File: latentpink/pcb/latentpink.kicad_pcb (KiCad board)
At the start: 8 copper layers, 145 x 139 mm, 563 parts, among them J1 CONN_SFP_HOST, J10 XILINX_JTAG, J13 CONN_01X05, J14 CONN_01X03, J15 CONN_01X03, J16 JUMPER_0402_SPDT, J17 JUMPER_0402_SPDT, J18 BEL_FUSE_0845-2R1T-E4, J19 BEL_FUSE_0845-2R1T-E4, J2 SFP_CAGE, J20 BEL_FUSE_0845-2R1T-E4, J21 BEL_FUSE_0845-2R1T-E4, J22 BEL_FUSE_0845-2R1T-E4, J3 XILINX_JTAG, J4 BEL_FUSE_0845-2R1T-E4, J5 0826-1G1T-23-F, J6 BARREL_JACK, J7 RJ45, J8 BEL_FUSE_0845-2R1T-E4, J9 XILINX_JTAG, M1 960-27-12-D-AB-0, M2 960-23-23-F-AB-0, M3 SCREWHOLE, M4 SCREWHOLE, M5 SCREWHOLE, M6 SCREWHOLE, U1 VSC8512, U10 MYMGK1R812ERSR, U11 MYMGK00504ERSR, U12 STM32L031-QFN32, U13 MYMGK00504ERSR, U14 MYMGK00504ERSR, U15 MYMGK00504ERSR, U16 NCP45521IMNTWG-H, U17 NCP45521IMNTWG-H, U18 LP2996AMRE, U19 TPS7A2533DRVR, U2 XC7K160T-2FBG484C, U20 AT24MAC402, U21 ECX2-LMV-3CN-125.000-TR, U22 ECS-2016MVQ-250-CN, U23 ADM3101E_QFN, U3 CY7C2245KV18-450BZXI, U4 STM32H735-UFBGA176-25, U5 DP83867, U6 DP83867, U9 KSZ9031RN

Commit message: Continued footprint assignment and miscellaneous missing tidbits of schematic
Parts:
- added C1: 330 uF, azonenberg_pcb:EIA_1210_CAP_NOSILK, F.Cu at (253.6, 36.1)
- added C100: 22 uF 25V, azonenberg_pcb:EIA_1812_CAP_NOSILK, F.Cu at (233.7, 72.2)
- added C101: 22 uF 25V, azonenberg_pcb:EIA_1812_CAP_NOSILK, F.Cu at (247.6, 56.2)
- added C102: 22 uF 25V, azonenberg_pcb:EIA_1812_CAP_NOSILK, F.Cu at (233.7, 56.2)
- added C103: 22 uF 25V, azonenberg_pcb:EIA_1812_CAP_NOSILK, F.Cu at (240.7, 56.2)
- added C104: 22 uF 25V, azonenberg_pcb:EIA_1812_CAP_NOSILK, F.Cu at (233.7, 60.2)
- added C105: 22 uF 25V, azonenberg_pcb:EIA_1812_CAP_NOSILK, F.Cu at (233.7, 68.2)
- added C107: 220 uF, azonenberg_pcb:EIA_1210_CAP_NOSILK, F.Cu at (232.6, 43.9)
- added C108: 220 uF, azonenberg_pcb:EIA_1210_CAP_NOSILK, F.Cu at (244.7, 72.0)
- added C109: 220 uF, azonenberg_pcb:EIA_1210_CAP_NOSILK, F.Cu at (246.6, 64.1)
- added C112: 220 uF, azonenberg_pcb:EIA_1210_CAP_NOSILK, F.Cu at (253.6, 56.1)
- added C113: 220 uF, azonenberg_pcb:EIA_1210_CAP_NOSILK, F.Cu at (234.5, 36.1)
- added C114: 220 uF, azonenberg_pcb:EIA_1210_CAP_NOSILK, F.Cu at (253.6, 60.0)
- added C117: EEH-ZS1E102UV, azonenberg_pcb:CAP_AL_10MM_SMT, F.Cu at (13.5, 24.3)
- added C118: DNP, azonenberg_pcb:CAP_AL_10MM_SMT, F.Cu at (13.4, 39.9)
- added C120: DNP, azonenberg_pcb:CAP_AL_10MM_SMT, F.Cu at (25.6, 39.9)
- added C122: EEH-ZS1E102UV, azonenberg_pcb:CAP_AL_10MM_SMT, F.Cu at (25.7, 24.3)
- added C154: 330 uF, azonenberg_pcb:EIA_1210_CAP_NOSILK, F.Cu at (237.7, 79.8)
- added C155: 47 uF, azonenberg_pcb:EIA_1210_CAP_NOSILK, F.Cu at (232.7, 83.7)
- added C157: 47 uF, azonenberg_pcb:EIA_1210_CAP_NOSILK, F.Cu at (232.7, 79.8)
- added C158: 330 uF, azonenberg_pcb:EIA_1210_CAP_NOSILK, F.Cu at (237.7, 83.7)
- added C159: 47 uF, azonenberg_pcb:EIA_1210_CAP_NOSILK, F.Cu at (242.7, 79.8)
- added C228: 0.47 uF, azonenberg_pcb:EIA_0402_CAP_NOSILK, F.Cu at (250.6, 48.0)
- added C229: 0.47 uF, azonenberg_pcb:EIA_0402_CAP_NOSILK, F.Cu at (215.7, 63.0)
- added C234: 4.7 uF, azonenberg_pcb:EIA_0603_CAP_NOSILK, F.Cu at (247.7, 46.7)
- added C241: 0.47 uF, azonenberg_pcb:EIA_0402_CAP_NOSILK, F.Cu at (250.6, 46.5)
- added C289: 47 uF, azonenberg_pcb:EIA_1210_CAP_NOSILK, F.Cu at (248.6, 36.1)
- added C301: 47 uF, azonenberg_pcb:EIA_1210_CAP_NOSILK, F.Cu at (253.6, 40.0)
- added C447: 0.47 uF, azonenberg_pcb:EIA_0402_CAP_NOSILK, F.Cu at (216.9, 60.6)
- added C448: 0.47 uF, azonenberg_pcb:EIA_0402_CAP_NOSILK, F.Cu at (193.8, 55.0)
- added C449: 0.47 uF, azonenberg_pcb:EIA_0402_CAP_NOSILK, F.Cu at (195.9, 61.1)
- added C450: 0.1 uF, azonenberg_pcb:EIA_0402_CAP_NOSILK, F.Cu at (139.3, 44.6)
- added C451: 0.1 uF, azonenberg_pcb:EIA_0402_CAP_NOSILK, F.Cu at (136.8, 41.6)
- added C452: 0.1 uF, azonenberg_pcb:EIA_0402_CAP_NOSILK, F.Cu at (139.3, 43.1)
- added C453: 0.1 uF, azonenberg_pcb:EIA_0402_CAP_NOSILK, F.Cu at (136.8, 44.6)
- added C454: 0.1 uF, azonenberg_pcb:EIA_0402_CAP_NOSILK, F.Cu at (141.8, 43.1)
- added C455: 0.1 uF, azonenberg_pcb:EIA_0402_CAP_NOSILK, F.Cu at (136.8, 43.1)
- added C456: 0.1 uF, azonenberg_pcb:EIA_0402_CAP_NOSILK, F.Cu at (141.8, 41.6)
- added C457: 0.1 uF, azonenberg_pcb:EIA_0402_CAP_NOSILK, F.Cu at (139.3, 41.6)
- added C458: 0.47 uF, azonenberg_pcb:EIA_0402_CAP_NOSILK, F.Cu at (189.8, 36.2)
- added C459: 0.47 uF, azonenberg_pcb:EIA_0402_CAP_NOSILK, F.Cu at (187.3, 36.2)
- added C460: 0.47 uF, azonenberg_pcb:EIA_0402_CAP_NOSILK, F.Cu at (187.3, 37.7)
- added C461: 0.47 uF, azonenberg_pcb:EIA_0402_CAP_NOSILK, F.Cu at (192.3, 34.7)
- added C462: 0.47 uF, azonenberg_pcb:EIA_0402_CAP_NOSILK, F.Cu at (187.3, 34.7)
- added C463: 0.47 uF, azonenberg_pcb:EIA_0402_CAP_NOSILK, F.Cu at (189.8, 37.7)
- added C464: 0.47 uF, azonenberg_pcb:EIA_0402_CAP_NOSILK, F.Cu at (187.3, 39.2)
- added C465: 0.47 uF, azonenberg_pcb:EIA_0402_CAP_NOSILK, F.Cu at (189.8, 34.7)
- added C466: 0.47 uF, azonenberg_pcb:EIA_0402_CAP_NOSILK, F.Cu at (238.1, 107.9)
- added C467: 0.1 uF, azonenberg_pcb:EIA_0402_CAP_NOSILK, F.Cu at (238.1, 109.4)
- added C468: 0.1 uF, azonenberg_pcb:EIA_0402_CAP_NOSILK, F.Cu at (235.6, 109.4)
- added C469: 0.1 uF, azonenberg_pcb:EIA_0402_CAP_NOSILK, F.Cu at (229.6, 114.8)
- added C470: 0.1 uF, azonenberg_pcb:EIA_0402_CAP_NOSILK, F.Cu at (232.1, 114.8)
- added C471: 22 uF, azonenberg_pcb:EIA_1206_CAP_NOSILK, F.Cu at (227.2, 108.4)
- added C472: 22 uF, azonenberg_pcb:EIA_1206_CAP_NOSILK, F.Cu at (227.2, 111.0)
- added C473: 0.1 uF, azonenberg_pcb:EIA_0402_CAP_NOSILK, F.Cu at (234.6, 112.5)
- added C474: 0.1 uF, azonenberg_pcb:EIA_0402_CAP_NOSILK, F.Cu at (225.9, 115.3)
- added C475: DNP, azonenberg_pcb:EIA_1210_CAP_NOSILK, F.Cu at (239.7, 68.1)
- added C476: DNP, azonenberg_pcb:EIA_1210_CAP_NOSILK, F.Cu at (249.7, 68.0)
- added C6: 47 uF, azonenberg_pcb:EIA_1206_CAP_NOSILK, F.Cu at (248.6, 39.4)
- added C67: 47 uF, azonenberg_pcb:EIA_1210_CAP_NOSILK, F.Cu at (240.0, 30.0)
- added C89: 22 uF 25V, azonenberg_pcb:EIA_1812_CAP_NOSILK, F.Cu at (240.7, 64.2)
- added C90: 22 uF 25V, azonenberg_pcb:EIA_1812_CAP_NOSILK, F.Cu at (240.7, 60.2)
- added C91: 220 uF, azonenberg_pcb:EIA_1210_CAP_NOSILK, F.Cu at (251.6, 64.1)
- added C92: 220 uF, azonenberg_pcb:EIA_1210_CAP_NOSILK, F.Cu at (239.7, 72.0)
- added C93: 220 uF, azonenberg_pcb:EIA_1210_CAP_NOSILK, F.Cu at (239.5, 36.1)
- added C94: 22 uF 25V, azonenberg_pcb:EIA_1812_CAP_NOSILK, F.Cu at (233.7, 64.2)
- added C95: 22 uF 25V, azonenberg_pcb:EIA_1812_CAP_NOSILK, F.Cu at (247.6, 60.2)
- added C96: 220 uF, azonenberg_pcb:EIA_1210_CAP_NOSILK, F.Cu at (244.7, 68.1)
- added C97: 220 uF, azonenberg_pcb:EIA_1210_CAP_NOSILK, F.Cu at (234.5, 40.0)
- added C98: 10 uF 25V, azonenberg_pcb:EIA_1210_CAP_NOSILK, F.Cu at (251.5, 79.8)
- added C99: 10 uF 25V, azonenberg_pcb:EIA_1210_CAP_NOSILK, F.Cu at (256.5, 79.8)
- added D5: GREEN, azonenberg_pcb:EIA_0603_LED, F.Cu at (214.0, 61.1)
- added D6: GREEN, azonenberg_pcb:EIA_0603_LED, F.Cu at (226.8, 120.4)
- added D7: GREEN, azonenberg_pcb:EIA_0603_LED, F.Cu at (226.8, 122.7)
- added J11: FAN_01, azonenberg_pcb:CONN_MOLEX_KK_0470531000, F.Cu at (107.4, 11.9)
- added J12: FAN_01, azonenberg_pcb:CONN_MOLEX_KK_0470531000, F.Cu at (95.2, 11.9)
- added L6: 4.7 uH, azonenberg_pcb:EIA_0805_INDUCTOR_NOSILK, F.Cu at (226.5, 113.5)
- added L7: 4.7 uH, azonenberg_pcb:EIA_0805_INDUCTOR_NOSILK, F.Cu at (231.5, 112.9)
- added M10: WEEE, w_logo:Logo_silk_WEEE_3.4x5mm, F.Cu at (229.5, 101.5)
- added M7: LONGTHING, azonenberg_pcb:LONGTHING-1200DPI, F.Cu at (222.7, 96.4)
- added M8: OSHW, w_logo:Logo_silk_OSHW_6x6mm, F.Cu at (230.5, 94.6)
- added M9: POLARITY, w_logo:Logo_silk_polarity_center_5x1.4mm, F.Cu at (220.1, 101.3)
- added R117: 100, azonenberg_pcb:EIA_0402_RES_NOSILK, F.Cu at (202.9, 61.1)
- added R118: 100, azonenberg_pcb:EIA_0402_RES_NOSILK, F.Cu at (202.9, 62.6)
- added R122: DNP, azonenberg_pcb:EIA_1206_CAP_NOSILK, F.Cu at (203.9, 35.2)
- added R123: 33, azonenberg_pcb:EIA_0402_RES_NOSILK, F.Cu at (207.1, 47.5)
- added R124: 33, azonenberg_pcb:EIA_0402_RES_NOSILK, F.Cu at (191.3, 55.0)
- added R125: 33, azonenberg_pcb:EIA_0402_RES_NOSILK, F.Cu at (193.8, 56.5)
- added R126: 33, azonenberg_pcb:EIA_0402_RES_NOSILK, F.Cu at (198.8, 55.0)
- added R127: 4.7K, azonenberg_pcb:EIA_0402_RES_NOSILK, F.Cu at (202.4, 52.1)
- added R128: 4.7K, azonenberg_pcb:EIA_0402_RES_NOSILK, F.Cu at (202.4, 53.6)
- added R129: 4.7K, azonenberg_pcb:EIA_0402_RES_NOSILK, F.Cu at (191.3, 56.5)
- added R130: 100, azonenberg_pcb:EIA_0402_RES_NOSILK, F.Cu at (195.9, 62.6)
- added R131: 100, azonenberg_pcb:EIA_0402_RES_NOSILK, F.Cu at (196.3, 55.0)
- added R132: 4.7K, azonenberg_pcb:EIA_0402_RES_NOSILK, F.Cu at (194.8, 34.7)
- added R133: 4.7K, azonenberg_pcb:EIA_0402_RES_NOSILK, F.Cu at (192.3, 36.2)
- added R134: 0.1, azonenberg_pcb:EIA_0402_RES_NOSILK, F.Cu at (235.6, 110.9)
- added R135: 0.5, azonenberg_pcb:EIA_0402_RES_NOSILK, F.Cu at (235.6, 107.9)
- added R136: 0.5, azonenberg_pcb:EIA_0402_RES_NOSILK, F.Cu at (234.6, 114.0)
- added R137: 5.76K, azonenberg_pcb:EIA_0402_RES_NOSILK, F.Cu at (228.4, 126.1)
- added R138: 2.49K, azonenberg_pcb:EIA_0402_RES_NOSILK, F.Cu at (230.9, 124.4)
- added R139: 10K, azonenberg_pcb:EIA_0402_RES_NOSILK, F.Cu at (232.2, 121.4)
- added R140: 2.49K, azonenberg_pcb:EIA_0402_RES_NOSILK, F.Cu at (225.9, 124.6)
- added R141: 5.76K, azonenberg_pcb:EIA_0402_RES_NOSILK, F.Cu at (234.7, 122.9)
- added R142: 2.49K, azonenberg_pcb:EIA_0402_RES_NOSILK, F.Cu at (229.7, 122.9)
- added R143: 10K, azonenberg_pcb:EIA_0402_RES_NOSILK, F.Cu at (237.2, 121.4)
- added R144: 2.49K, azonenberg_pcb:EIA_0402_RES_NOSILK, F.Cu at (230.9, 125.9)
- added R145: 10K, azonenberg_pcb:EIA_0402_RES_NOSILK, F.Cu at (229.7, 119.9)
- added R146: 2.49K, azonenberg_pcb:EIA_0402_RES_NOSILK, F.Cu at (233.4, 124.4)
- added R147: 10K, azonenberg_pcb:EIA_0402_RES_NOSILK, F.Cu at (234.7, 119.9)
- added R148: 2.49K, azonenberg_pcb:EIA_0402_RES_NOSILK, F.Cu at (237.2, 119.9)
- added R149: 470, azonenberg_pcb:EIA_0402_RES_NOSILK, F.Cu at (228.4, 124.6)
- added R150: 470, azonenberg_pcb:EIA_0402_RES_NOSILK, F.Cu at (229.7, 121.4)
- added R151: 470, azonenberg_pcb:EIA_0402_RES_NOSILK, F.Cu at (232.2, 122.9)
- added R152: 470, azonenberg_pcb:EIA_0402_RES_NOSILK, F.Cu at (234.7, 121.4)
- added R153: 470, azonenberg_pcb:EIA_0402_RES_NOSILK, F.Cu at (225.9, 126.1)
- added R154: 470, azonenberg_pcb:EIA_0402_RES_NOSILK, F.Cu at (232.2, 119.9)
- added R53: 470, azonenberg_pcb:EIA_0402_RES_NOSILK, F.Cu at (213.2, 63.0)
- added TP19: TESTPOINT, azonenberg_pcb:TESTPOINT_SMT_0.5MM, F.Cu at (222.8, 60.6)
- added TP20: TESTPOINT, azonenberg_pcb:TESTPOINT_SMT_0.5MM, F.Cu at (222.8, 62.1)
- added TP21: TESTPOINT, azonenberg_pcb:TESTPOINT_SMT_0.5MM, F.Cu at (204.9, 61.1)
- added TP22: TESTPOINT, azonenberg_pcb:TESTPOINT_SMT_0.5MM, F.Cu at (204.9, 62.6)
- added TP23: U.FL, azonenberg_pcb:CONN_U.FL_TE_1909763-1, F.Cu at (225.8, 49.3)
- added TP24: U.FL, azonenberg_pcb:CONN_U.FL_TE_1909763-1, F.Cu at (214.7, 49.3)
- added TP25: U.FL, azonenberg_pcb:CONN_U.FL_TE_1909763-1, F.Cu at (220.3, 49.3)
- added U24: SIT9121AI-2BF-XXS200.000000G, azonenberg_pcb:OSCILLATOR_LVDS_3.2x2.5, F.Cu at (105.4, 76.6)
- added U25: SIT9121AI-2BF-XXS156.250000G, azonenberg_pcb:OSCILLATOR_LVDS_3.2x2.5, F.Cu at (100.8, 76.6)
- added U26: 74LVC1T45, azonenberg_pcb:DFN_6_0.5MM_1.45x1.00MM, F.Cu at (87.7, 134.2)
- added U27: 74LVC1T45, azonenberg_pcb:DFN_6_0.5MM_1.45x1.00MM, F.Cu at (90.2, 134.2)
- added U28: IS25WP256D-JLLE, azonenberg_pcb:DFN_8_1.27MM_8x6MM, F.Cu at (195.6, 50.5)
- added U29: DSC1123CI2-150.0000T, azonenberg_pcb:OSCILLATOR_LVDS_3.2x2.5, F.Cu at (203.5, 49.1)
- added U30: DSC1123CI2-150.0000T, azonenberg_pcb:OSCILLATOR_LVDS_3.2x2.5, F.Cu at (192.4, 62.7)
- added U31: 74LVC1T45, azonenberg_pcb:DFN_6_0.5MM_1.45x1.00MM, F.Cu at (194.9, 38.6)
- added U32: 74LVC1T45, azonenberg_pcb:DFN_6_0.5MM_1.45x1.00MM, F.Cu at (194.9, 36.4)
- added U33: 74LVC1T45, azonenberg_pcb:DFN_6_0.5MM_1.45x1.00MM, F.Cu at (189.9, 39.4)
- added U34: 74LVC1T45, azonenberg_pcb:DFN_6_0.5MM_1.45x1.00MM, F.Cu at (192.4, 37.9)
- added U35: SIT9121AC-2B2-33E125.000000, azonenberg_pcb:OSCILLATOR_LVDS_3.2x2.5, F.Cu at (232.0, 109.5)
- added U7: ECS-1612MV-250-CN-TR, azonenberg_pcb:OSCILLATOR_1.6x1.2, F.Cu at (122.9, 30.1)
- added U8: ECS-1612MV-250-CN-TR, azonenberg_pcb:OSCILLATOR_1.6x1.2, F.Cu at (120.8, 48.6)
- moved R115 5.04 mm to (124.7, 28.2)
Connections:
- C190 pad 1: unconnected-(C190-Pad1) -> /3V3
- C190 pad 2: unconnected-(C190-Pad2) -> /GND
- C340 pad 1: unconnected-(C340-Pad1) -> Net-(C340-Pad1)
- C340 pad 2: unconnected-(C340-Pad2) -> /QSGMII PHY/GTX_REFCLK_SPARE_P
- C341 pad 1: unconnected-(C341-Pad1) -> Net-(C341-Pad1)
- C341 pad 2: unconnected-(C341-Pad2) -> /QSGMII PHY/GTX_REFCLK_SPARE_N
- C342 pad 1: unconnected-(C342-Pad1) -> Net-(C342-Pad1)
- C342 pad 2: unconnected-(C342-Pad2) -> /QSGMII PHY/GTX_REFCLK_156M25_P
- C343 pad 1: unconnected-(C343-Pad1) -> Net-(C343-Pad1)
- C343 pad 2: unconnected-(C343-Pad2) -> /QSGMII PHY/GTX_REFCLK_156M25_N
- C344 pad 1: unconnected-(C344-Pad1) -> /3V3
- C344 pad 2: unconnected-(C344-Pad2) -> /GND
- C345 pad 1: unconnected-(C345-Pad1) -> /3V3
- C345 pad 2: unconnected-(C345-Pad2) -> /GND
- C355 pad 1: /SGMII PHYs/1V8_IO -> /1V8_IO
- C356 pad 1: /SGMII PHYs/1V8_IO -> /1V8_IO
- C360 pad 1: /SGMII PHYs/1V8_IO -> /1V8_IO
- C364 pad 1: /SGMII PHYs/1V8_IO -> /1V8_IO
- C368 pad 1: /SGMII PHYs/1V8_IO -> /1V8_IO
- C372 pad 1: /SGMII PHYs/1V8_IO -> /1V8_IO
- C375 pad 1: /SGMII PHYs/1V8_IO -> /1V8_IO
- C378 pad 1: /SGMII PHYs/1V8_IO -> /1V8_IO
- C382 pad 1: /SGMII PHYs/1V8_IO -> /1V8_IO
- C384 pad 1: /SGMII PHYs/1V8_IO -> /1V8_IO
- J22 pad 12: unconnected-(J22-Pad12) -> /SGMII PHYs/ETH13_B_TAP
- J22 pad 14: unconnected-(J22-Pad14) -> /SGMII PHYs/ETH12_A_TAP
- J22 pad 17: unconnected-(J22-Pad17) -> /SGMII PHYs/ETH12_C_TAP
- J22 pad 22: unconnected-(J22-Pad22) -> /SGMII PHYs/ETH12_B_TAP
- J22 pad 25: unconnected-(J22-Pad25) -> /SGMII PHYs/ETH12_D_TAP
- J22 pad 27: unconnected-(J22-Pad27) -> /GND
- J22 pad 28: unconnected-(J22-Pad28) -> Net-(J22-Pad28)
- J22 pad 29: unconnected-(J22-Pad29) -> /GND
- J22 pad 30: unconnected-(J22-Pad30) -> Net-(J22-Pad30)
- J22 pad 31: unconnected-(J22-Pad31) -> /GND
- J22 pad 32: unconnected-(J22-Pad32) -> Net-(J22-Pad32)
- J22 pad 33: unconnected-(J22-Pad33) -> /GND
- J22 pad 34: unconnected-(J22-Pad34) -> Net-(J22-Pad34)
- J22 pad 4: unconnected-(J22-Pad4) -> /SGMII PHYs/ETH13_C_TAP
- J22 pad 7: unconnected-(J22-Pad7) -> /SGMII PHYs/ETH13_A_TAP
- J22 pad 8: unconnected-(J22-Pad8) -> /SGMII PHYs/ETH13_D_TAP
- U1 pad AA8: unconnected-(U1-PadAA8) -> /QSGMII PHY/PHY_REFCLK_125MHZ_N
- U1 pad Y8: unconnected-(U1-PadY8) -> /QSGMII PHY/PHY_REFCLK_125MHZ_P
- U12 pad 16: /FPGA/FPGA_DONE -> /Power Supply/FPGA_DONE_3V3
- U12 pad 26: /FPGA/FPGA_INIT -> /Power Supply/FPGA_INIT_3V3
- U12 pad 3: unconnected-(U12-Pad3) -> /Power Supply/SUPER_GPIO
- U2 pad AA10: unconnected-(U2-PadAA10) -> /SGMII PHYs/ETH13_SGMII_TX_AC_P
- U2 pad AA8: unconnected-(U2-PadAA8) -> /SGMII PHYs/ETH13_SGMII_RX_AC_N
- U2 pad AA9: unconnected-(U2-PadAA9) -> /SGMII PHYs/ETH13_SGMII_RX_AC_P
- U2 pad AB10: unconnected-(U2-PadAB10) -> /SGMII PHYs/ETH13_SGMII_TX_AC_N
- U2 pad P17: unconnected-(U2-PadP17) -> /FPGA/QDR SRAM/I2C_DERP_SCL
- U2 pad P21: unconnected-(U2-PadP21) -> /FPGA/QDR SRAM/I2C_DERP_SDA
- U2 pad P22: unconnected-(U2-PadP22) -> /FPGA/QDR SRAM/I2C_DERP_SCL
- U2 pad R17: unconnected-(U2-PadR17) -> /FPGA/QDR SRAM/I2C_DERP_SDA
- U2 pad R6: unconnected-(U2-PadR6) -> /SGMII PHYs/ETH12_LED0_1V8
- U2 pad R7: unconnected-(U2-PadR7) -> /SGMII PHYs/ETH12_LED1_1V8
- U2 pad T10: unconnected-(U2-PadT10) -> /SGMII PHYs/ETH12_GPIO_0
- U2 pad T11: unconnected-(U2-PadT11) -> /QSGMII PHY/VSC_MDC_1V8
- U2 pad T9: unconnected-(U2-PadT9) -> /SGMII PHYs/ETH13_GPIO_0
- U2 pad U10: unconnected-(U2-PadU10) -> /QSGMII PHY/VSC_FAST_STATUS_1V8
- U2 pad U11: unconnected-(U2-PadU11) -> /SGMII PHYs/ETH13_GPIO_1
- U2 pad U12: unconnected-(U2-PadU12) -> /SGMII PHYs/ETH12_GPIO_1
- U2 pad V10: unconnected-(U2-PadV10) -> /QSGMII PHY/VSC_MDIO_1V8
- U2 pad V9: unconnected-(U2-PadV9) -> /QSGMII PHY/VSC_MDINT_1V8
- U2 pad W10: unconnected-(U2-PadW10) -> /QSGMII PHY/VSC_MDIO_OE
- U2 pad W11: unconnected-(U2-PadW11) -> /SGMII PHYs/ETH13_LED2_1V8
- U2 pad W6: unconnected-(U2-PadW6) -> /SGMII PHYs/ETH13_LED0_1V8
- U2 pad W9: unconnected-(U2-PadW9) -> /SGMII PHYs/ETH13_SGMII_CLKOUT_AC_P
- U2 pad Y11: unconnected-(U2-PadY11) -> /SGMII PHYs/ETH13_LED1_1V8
- U2 pad Y6: unconnected-(U2-PadY6) -> /SGMII PHYs/ETH12_LED2_1V8
- U2 pad Y9: unconnected-(U2-PadY9) -> /SGMII PHYs/ETH13_SGMII_CLKOUT_AC_N
- U5 pad 19: /SGMII PHYs/1V8_IO -> /1V8_IO
- U5 pad 30: /SGMII PHYs/1V8_IO -> /1V8_IO
- U5 pad 39: unconnected-(U5-Pad39) -> /SGMII PHYs/ETH13_GPIO_0
- U5 pad 40: unconnected-(U5-Pad40) -> /SGMII PHYs/ETH13_GPIO_1
- U5 pad 41: /SGMII PHYs/1V8_IO -> /1V8_IO
- U5 pad 45: unconnected-(U5-Pad45) -> /SGMII PHYs/ETH13_LED2_1V8
- U5 pad 46: unconnected-(U5-Pad46) -> /SGMII PHYs/ETH13_LED1_1V8
- U5 pad 47: unconnected-(U5-Pad47) -> /SGMII PHYs/ETH13_LED0_1V8
- U6 pad 19: /SGMII PHYs/1V8_IO -> /1V8_IO
- U6 pad 30: /SGMII PHYs/1V8_IO -> /1V8_IO
- U6 pad 39: unconnected-(U6-Pad39) -> /SGMII PHYs/ETH12_GPIO_0
- U6 pad 40: unconnected-(U6-Pad40) -> /SGMII PHYs/ETH12_GPIO_1
- U6 pad 41: /SGMII PHYs/1V8_IO -> /1V8_IO
- U6 pad 45: unconnected-(U6-Pad45) -> /SGMII PHYs/ETH12_LED2_1V8
- U6 pad 46: unconnected-(U6-Pad46) -> /SGMII PHYs/ETH12_LED1_1V8
- U6 pad 47: unconnected-(U6-Pad47) -> /SGMII PHYs/ETH12_LED0_1V8

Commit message: Finished initial schematic, ready for design review
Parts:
- removed R49: 10K, azonenberg_pcb:EIA_0402_RES_NOSILK
- added C156: 100 uF, azonenberg_pcb:EIA_1206_CAP_NOSILK, F.Cu at (192.5, 146.5)
- added C160: 100 uF, azonenberg_pcb:EIA_1206_CAP_NOSILK, F.Cu at (192.5, 149.1)
- added C161: 100 uF, azonenberg_pcb:EIA_1206_CAP_NOSILK, F.Cu at (197.5, 146.5)
- added C169: 22 uF, azonenberg_pcb:EIA_1206_CAP_NOSILK, F.Cu at (212.5, 146.5)
- added C171: 220 uF, azonenberg_pcb:EIA_1210_CAP_NOSILK, F.Cu at (207.5, 147.2)
- added C173: 2.2 uF, azonenberg_pcb:EIA_0805_CAP_NOSILK, F.Cu at (237.7, 104.1)
- added C174: 2.2 uF, azonenberg_pcb:EIA_0805_CAP_NOSILK, F.Cu at (241.3, 104.1)
- added C177: 47 uF, azonenberg_pcb:EIA_1206_CAP_NOSILK, F.Cu at (206.8, 156.2)
- added C178: 47 uF, azonenberg_pcb:EIA_1206_CAP_NOSILK, F.Cu at (206.8, 158.8)
- added C217: 10 uF, azonenberg_pcb:EIA_0805_CAP_NOSILK, F.Cu at (218.9, 155.7)
- added C218: 220 pF, azonenberg_pcb:EIA_0402_CAP_NOSILK, F.Cu at (237.1, 144.4)
- added C221: 10 uF, azonenberg_pcb:EIA_0805_CAP_NOSILK, F.Cu at (222.5, 155.7)
- added C262: 22 uF, azonenberg_pcb:EIA_0805_CAP_NOSILK, F.Cu at (195.4, 158.8)
- added C263: 22 uF, azonenberg_pcb:EIA_0805_CAP_NOSILK, F.Cu at (191.8, 158.8)
- added C265: 22 uF, azonenberg_pcb:EIA_0805_CAP_NOSILK, F.Cu at (199.0, 158.8)
- added C283: 22 uF, azonenberg_pcb:EIA_1206_CAP_NOSILK, F.Cu at (192.5, 156.2)
- added C284: 22 uF, azonenberg_pcb:EIA_0805_CAP_NOSILK, F.Cu at (196.8, 156.2)
- added C352: 1 uF, azonenberg_pcb:EIA_0402_CAP_NOSILK, F.Cu at (250.9, 103.5)
- added C353: 1 uF, azonenberg_pcb:EIA_0402_CAP_NOSILK, F.Cu at (248.4, 105.0)
- added C354: 1 uF, azonenberg_pcb:EIA_0402_CAP_NOSILK, F.Cu at (248.4, 103.5)
- added C477: 22 uF, azonenberg_pcb:EIA_1206_CAP_NOSILK, F.Cu at (196.9, 9.00)
- added C478: 22 uF, azonenberg_pcb:EIA_1206_CAP_NOSILK, F.Cu at (201.9, 9.00)
- added C479: 22 uF, azonenberg_pcb:EIA_1206_CAP_NOSILK, F.Cu at (196.9, 14.2)
- added C480: 22 uF, azonenberg_pcb:EIA_1206_CAP_NOSILK, F.Cu at (196.9, 11.6)
- added FB10: CIS21J121NE, azonenberg_pcb:EIA_0805_INDUCTOR_NOSILK, F.Cu at (201.2, 11.4)
- added FB11: CIS21J121NE, azonenberg_pcb:EIA_0805_INDUCTOR_NOSILK, F.Cu at (206.2, 8.81)
- added FB2: BLM31KN271SH1L, azonenberg_pcb:EIA_1206_CAP_NOSILK, F.Cu at (191.3, 26.8)
- added FB3: BLM31KN271SH1L, azonenberg_pcb:EIA_1206_CAP_NOSILK, F.Cu at (191.3, 24.2)
- added FB4: BLM31KN271SH1L, azonenberg_pcb:EIA_1206_CAP_NOSILK, F.Cu at (196.3, 24.2)
- added FB9: MMZ1005S102CT000, azonenberg_pcb:EIA_0402_CAP_NOSILK, F.Cu at (214.7, 8.46)
- added L1: 2.2 uH, azonenberg_pcb:EIA_1210_CAP_NOSILK, F.Cu at (108.1, 118.3)
- added R1: 16K, azonenberg_pcb:EIA_0402_RES_NOSILK, F.Cu at (230.9, 144.4)
- added R105: 620 1%, azonenberg_pcb:EIA_0402_RES_NOSILK, F.Cu at (225.9, 139.8)
- added R108: 1K, azonenberg_pcb:EIA_0402_RES_NOSILK, F.Cu at (228.4, 136.8)
- added R109: 2K 1%, azonenberg_pcb:EIA_0402_RES_NOSILK, F.Cu at (228.4, 138.2)
- added R11: 160, azonenberg_pcb:EIA_0402_RES_NOSILK, F.Cu at (228.4, 144.4)
- added R110: 2K 1%, azonenberg_pcb:EIA_0402_RES_NOSILK, F.Cu at (225.9, 136.8)
- added R111: 2K 1%, azonenberg_pcb:EIA_0402_RES_NOSILK, F.Cu at (225.9, 138.2)
- added R112: 1.5K, azonenberg_pcb:EIA_0402_RES_NOSILK, F.Cu at (239.7, 136.8)
- added R113: 2.2K, azonenberg_pcb:EIA_0402_RES_NOSILK, F.Cu at (239.7, 138.2)
- added R114: 11K 1%, azonenberg_pcb:EIA_0402_RES_NOSILK, F.Cu at (242.2, 136.8)
- added R119: 1.5K, azonenberg_pcb:EIA_0402_RES_NOSILK, F.Cu at (237.2, 136.8)
- added R12: 22, azonenberg_pcb:EIA_0402_RES_NOSILK, F.Cu at (228.4, 147.4)
- added R120: 2.2K, azonenberg_pcb:EIA_0402_RES_NOSILK, F.Cu at (242.2, 138.2)
- added R121: 11K 1%, azonenberg_pcb:EIA_0402_RES_NOSILK, F.Cu at (237.2, 138.2)
- added R13: 300, azonenberg_pcb:EIA_0402_RES_NOSILK, F.Cu at (225.9, 144.4)
- added R39: 10K, azonenberg_pcb:EIA_0402_RES_NOSILK, F.Cu at (228.4, 145.9)
- added R47: 249, azonenberg_pcb:EIA_0402_RES_NOSILK, F.Cu at (247.8, 136.8)
- added R8: 3k, azonenberg_pcb:EIA_0402_RES_NOSILK, F.Cu at (225.9, 145.9)
- added R9: 2.2k, azonenberg_pcb:EIA_0402_RES_NOSILK, F.Cu at (225.9, 147.4)
- added RN1: YC124-FR-0749R9L, azonenberg_pcb:YAGEO_YC124-FR, F.Cu at (27.2, 79.7)
- added RN2: YC124-FR-0749R9L, azonenberg_pcb:YAGEO_YC124-FR, F.Cu at (32.8, 79.7)
- added RN3: YC124-FR-0749R9L, azonenberg_pcb:YAGEO_YC124-FR, F.Cu at (30.0, 82.5)
- added RN4: YC124-FR-0749R9L, azonenberg_pcb:YAGEO_YC124-FR, F.Cu at (30.0, 79.7)
- added RN5: YC124-FR-0749R9L, azonenberg_pcb:YAGEO_YC124-FR, F.Cu at (32.8, 82.5)
- added RN6: YC124-FR-0749R9L, azonenberg_pcb:YAGEO_YC124-FR, F.Cu at (27.2, 82.5)
- added TP26: U.FL, azonenberg_pcb:CONN_U.FL_TE_1909763-1, F.Cu at (191.6, 10.3)
- added TP27: U.FL, azonenberg_pcb:CONN_U.FL_TE_1909763-1, F.Cu at (191.6, 15.6)
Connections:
- C458 pad 1: /QSGMII PHY/1V8_IO -> /1V8_IO
- C459 pad 1: /QSGMII PHY/1V8_IO -> /1V8_IO
- C460 pad 1: /QSGMII PHY/1V8_IO -> /1V8_IO
- C461 pad 1: /QSGMII PHY/1V8_IO -> /1V8_IO
- J22 pad 15: /SGMII PHYs/ETH12_A_N -> /SGMII PHYs/ETH12_A_P
- R149 pad 1: /SGMII PHYs/ETH12_LED0_3V3 -> /Management/ETH12_LED0_3V3
- R150 pad 1: /SGMII PHYs/ETH12_LED1_3V3 -> /Management/ETH12_LED1_3V3
- R151 pad 1: /SGMII PHYs/ETH13_LED0_3V3 -> /Management/ETH13_LED0_3V3
- R152 pad 1: /SGMII PHYs/ETH13_LED1_3V3 -> /Management/ETH13_LED1_3V3
- R153 pad 1: /SGMII PHYs/ETH12_LED2_3V3 -> /Management/ETH12_LED2_3V3
- R154 pad 1: /SGMII PHYs/ETH13_LED2_3V3 -> /Management/ETH13_LED2_3V3
- R33 pad 1: /Power Supply/1V0_RAW -> /1V0
- R33 pad 2: /1V0 -> /Power Supply/1V0_RAW
- R34 pad 1: /Power Supply/1V2_RAW -> /1V2
- R34 pad 2: /1V2 -> /Power Supply/1V2_RAW
- R36 pad 1: /Power Supply/2V5_RAW -> /2V5
- R36 pad 2: /2V5 -> /Power Supply/2V5_RAW
- R37 pad 1: /Power Supply/3V3_RAW -> /3V3
- R37 pad 2: /3V3 -> /Power Supply/3V3_RAW
- R38 pad 1: /Power Supply/1V8_RAW -> /1V8
- R38 pad 2: /1V8 -> /Power Supply/1V8_RAW
- U12 pad 27: /Power Supply/MCU_HEARTBEAT -> /Management/MCU_HEARTBEAT
- U12 pad 28: /Power Supply/HARD_RESET_REQ -> /Management/HARD_RESET_REQ
- U2 pad E9: unconnected-(U2-PadE9) -> /Management/ETH12_LED2_3V3
- U2 pad F9: unconnected-(U2-PadF9) -> /Management/ETH12_LED1_3V3
- U2 pad G12: unconnected-(U2-PadG12) -> /Management/ETH12_LED0_3V3
- U2 pad G8: unconnected-(U2-PadG8) -> /Management/ETH13_LED2_3V3
- U2 pad H8: unconnected-(U2-PadH8) -> /Management/ETH13_LED1_3V3
- U2 pad H9: unconnected-(U2-PadH9) -> /Management/ETH13_LED0_3V3
- U31 pad 1: /QSGMII PHY/1V8_IO -> /1V8_IO
- U32 pad 1: /QSGMII PHY/1V8_IO -> /1V8_IO
- U33 pad 1: /QSGMII PHY/1V8_IO -> /1V8_IO
- U33 pad 5: /QSGMII PHY/1V8_IO -> /1V8_IO
- U34 pad 1: /QSGMII PHY/1V8_IO -> /1V8_IO
- U4 pad A13: /Management/MCU_VSMPS -> /Management/VSMPS
- U4 pad A3: /Management/MCU_VSMPS -> /Management/VSMPS
- U4 pad K14: unconnected-(U4-PadK14) -> /Management/MCU_HEARTBEAT
- U4 pad K15: unconnected-(U4-PadK15) -> /Management/HARD_RESET_REQ
- U4 pad R14: /Management/MCU_VSMPS -> /Management/VSMPS

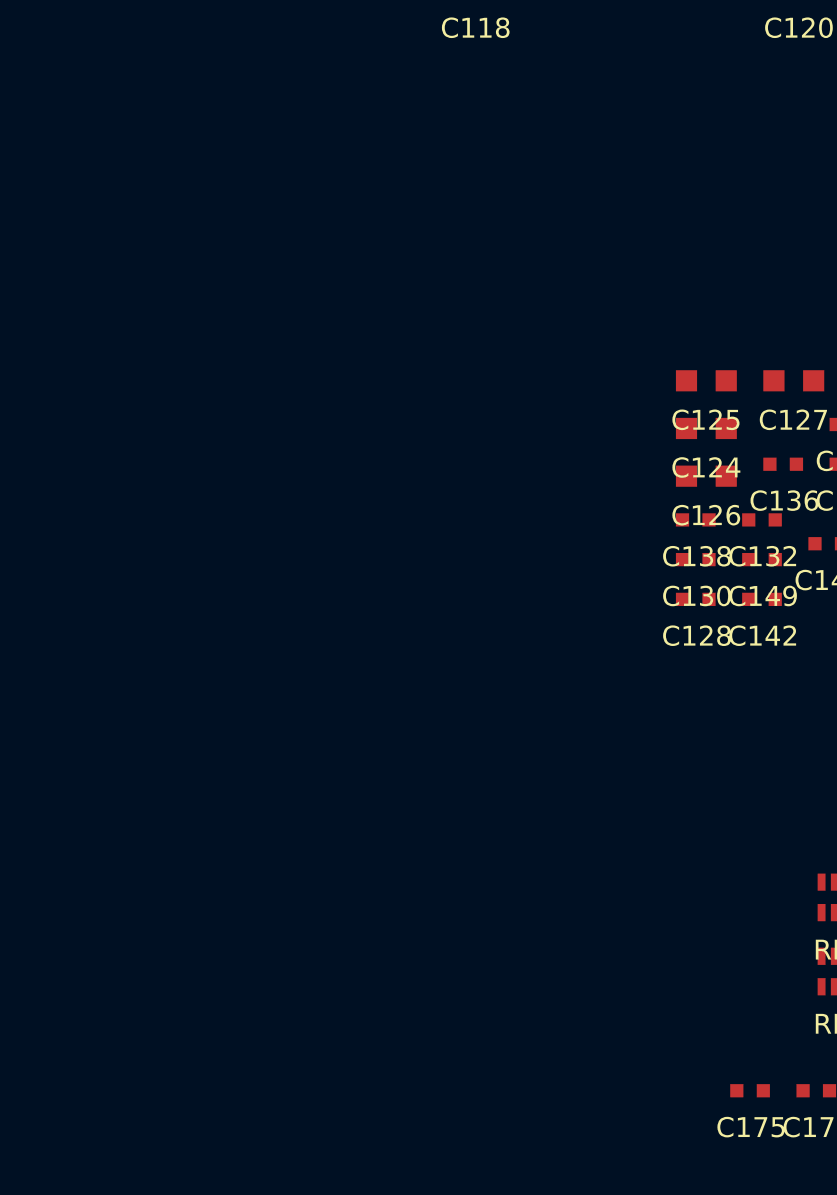
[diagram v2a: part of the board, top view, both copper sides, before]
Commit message: Added some debug LEDs, PMOD, and temp sensors
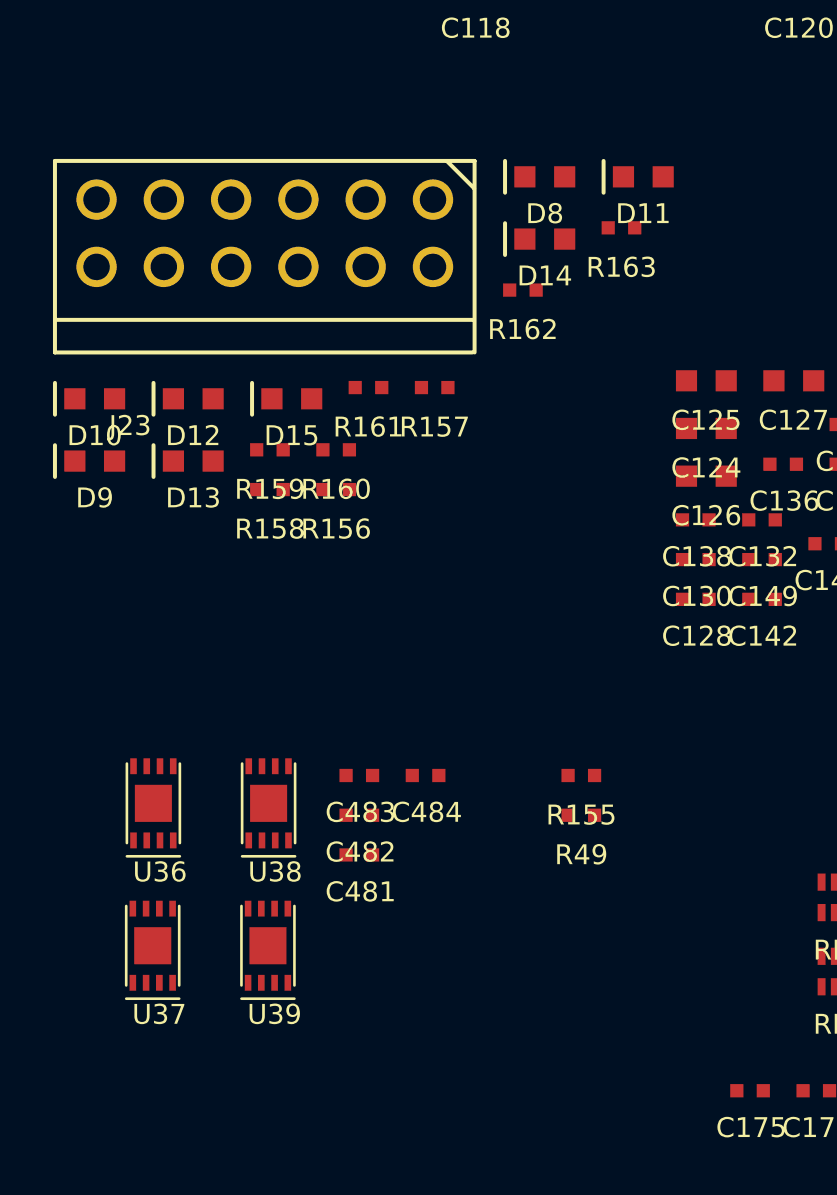
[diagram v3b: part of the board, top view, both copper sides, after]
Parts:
- added C481: 0.47 uF, azonenberg_pcb:EIA_0402_CAP_NOSILK, F.Cu at (9.00, 78.1)
- added C482: 0.47 uF, azonenberg_pcb:EIA_0402_CAP_NOSILK, F.Cu at (9.00, 76.6)
- added C483: 0.47 uF, azonenberg_pcb:EIA_0402_CAP_NOSILK, F.Cu at (9.00, 75.1)
- added C484: 0.47 uF, azonenberg_pcb:EIA_0402_CAP_NOSILK, F.Cu at (11.5, 75.1)
- added D10: GREEN, azonenberg_pcb:EIA_0603_LED, F.Cu at (-0.99, 60.9)
- added D11: GREEN, azonenberg_pcb:EIA_0603_LED, F.Cu at (19.7, 52.5)
- added D12: GREEN, azonenberg_pcb:EIA_0603_LED, F.Cu at (2.73, 60.9)
- added D13: GREEN, azonenberg_pcb:EIA_0603_LED, F.Cu at (2.73, 63.2)
- added D14: GREEN, azonenberg_pcb:EIA_0603_LED, F.Cu at (16.0, 54.9)
- added D15: GREEN, azonenberg_pcb:EIA_0603_LED, F.Cu at (6.45, 60.9)
- added D8: GREEN, azonenberg_pcb:EIA_0603_LED, F.Cu at (16.0, 52.5)
- added D9: GREEN, azonenberg_pcb:EIA_0603_LED, F.Cu at (-0.99, 63.2)
- added J23: PMOD_HOST, azonenberg_pcb:CONN_HEADER_2.54MM_2x6_RA_PMOD_HOST, F.Cu at (5.43, 54.6)
- added R155: 4.7K, azonenberg_pcb:EIA_0402_RES_NOSILK, F.Cu at (17.4, 75.1)
- added R156: 470, azonenberg_pcb:EIA_0402_RES_NOSILK, F.Cu at (8.12, 64.3)
- added R157: 470, azonenberg_pcb:EIA_0402_RES_NOSILK, F.Cu at (11.8, 60.5)
- added R158: 470, azonenberg_pcb:EIA_0402_RES_NOSILK, F.Cu at (5.62, 64.3)
- added R159: 470, azonenberg_pcb:EIA_0402_RES_NOSILK, F.Cu at (5.62, 62.8)
- added R160: 470, azonenberg_pcb:EIA_0402_RES_NOSILK, F.Cu at (8.12, 62.8)
- added R161: 470, azonenberg_pcb:EIA_0402_RES_NOSILK, F.Cu at (9.35, 60.5)
- added R162: 470, azonenberg_pcb:EIA_0402_RES_NOSILK, F.Cu at (15.2, 56.8)
- added R163: 470, azonenberg_pcb:EIA_0402_RES_NOSILK, F.Cu at (18.9, 54.4)
- added R49: 4.7K, azonenberg_pcb:EIA_0402_RES_NOSILK, F.Cu at (17.4, 76.6)
- added U36: AT30TS74_UDFN, azonenberg_pcb:DFN_8_0.5MM_2x3MM_TALL, F.Cu at (1.23, 76.2)
- added U37: AT30TS74_UDFN, azonenberg_pcb:DFN_8_0.5MM_2x3MM_TALL, F.Cu at (1.20, 81.5)
- added U38: AT30TS74_UDFN, azonenberg_pcb:DFN_8_0.5MM_2x3MM_TALL, F.Cu at (5.58, 76.2)
- added U39: AT30TS74_UDFN, azonenberg_pcb:DFN_8_0.5MM_2x3MM_TALL, F.Cu at (5.55, 81.5)
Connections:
- U2 pad B10: unconnected-(U2-PadB10) -> /Management/PMOD_DQ7
- U2 pad B11: unconnected-(U2-PadB11) -> /Management/PMOD_DQ6
- U2 pad C9: unconnected-(U2-PadC9) -> /Management/PMOD_DQ5
- U2 pad D9: unconnected-(U2-PadD9) -> /Management/PMOD_DQ4
- U2 pad E13: unconnected-(U2-PadE13) -> /Management/FPGA_LED3
- U2 pad F13: unconnected-(U2-PadF13) -> /Management/FPGA_LED0
- U2 pad G10: unconnected-(U2-PadG10) -> /Management/PMOD_DQ1
- U2 pad G11: unconnected-(U2-PadG11) -> /Management/PMOD_DQ0
- U2 pad H10: unconnected-(U2-PadH10) -> /Management/PMOD_DQ3
- U2 pad H12: unconnected-(U2-PadH12) -> /Management/PMOD_DQ2
- U2 pad H13: unconnected-(U2-PadH13) -> /Management/FPGA_LED2
- U2 pad H14: unconnected-(U2-PadH14) -> /Management/FPGA_LED1
- U4 pad A5: unconnected-(U4-PadA5) -> /TEMP_I2C_SCL
- U4 pad B11: unconnected-(U4-PadB11) -> /Management/MCU_LED0
- U4 pad B5: unconnected-(U4-PadB5) -> /TEMP_I2C_SDA
- U4 pad C1: unconnected-(U4-PadC1) -> /Management/MCU_LED1
- U4 pad D1: unconnected-(U4-PadD1) -> /Management/MCU_LED3
- U4 pad D2: unconnected-(U4-PadD2) -> /Management/MCU_LED2

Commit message: Continued work on signoff review, added some more test points and SFP+ activity LEDs
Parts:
- added D16: GREEN, azonenberg_pcb:EIA_0603_LED, F.Cu at (25.0, 154.0)
- added D17: GREEN, azonenberg_pcb:EIA_0603_LED, F.Cu at (25.0, 151.7)
- added R164: 470, azonenberg_pcb:EIA_0402_RES_NOSILK, F.Cu at (24.2, 155.9)
- added R165: 470, azonenberg_pcb:EIA_0402_RES_NOSILK, F.Cu at (27.9, 151.2)
- added R166: 0, azonenberg_pcb:EIA_0402_RES_NOSILK, F.Cu at (33.5, 151.2)
- added TP28: U.FL, azonenberg_pcb:CONN_U.FL_TE_1909763-1, F.Cu at (20.1, 153.1)
- added TP29: U.FL, azonenberg_pcb:CONN_U.FL_TE_1909763-1, F.Cu at (256.5, 116.5)
- added TP30: U.FL, azonenberg_pcb:CONN_U.FL_TE_1909763-1, F.Cu at (250.9, 116.5)
- added TP31: U.FL, azonenberg_pcb:CONN_U.FL_TE_1909763-1, F.Cu at (245.4, 116.5)
- added TP32: GROUNDCLIP, azonenberg_pcb:TESTPOINT_SMT_KEYSTONE_5016, F.Cu at (272.3, 116.1)
- added TP33: GROUNDCLIP, azonenberg_pcb:TESTPOINT_SMT_KEYSTONE_5016, F.Cu at (266.6, 116.1)
- added TP34: GROUNDCLIP, azonenberg_pcb:TESTPOINT_SMT_KEYSTONE_5016, F.Cu at (266.6, 120.6)
- added TP35: GROUNDCLIP, azonenberg_pcb:TESTPOINT_SMT_KEYSTONE_5016, F.Cu at (272.3, 120.6)
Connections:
- U11 pad 5: /1V2 -> /Power Supply/1V2_SENSE
- U2 pad E12: unconnected-(U2-PadE12) -> /Management/SFP_LED0
- U2 pad F11: unconnected-(U2-PadF11) -> /Management/SFP_LED1
- U2 pad H20: unconnected-(U2-PadH20) -> /FPGA/QDR SRAM/QDR_SYSCLK_N
- U2 pad J20: unconnected-(U2-PadJ20) -> /FPGA/QDR SRAM/QDR_SYSCLK_P
- U2 pad L20: /FPGA/QDR SRAM/QDR_CQ_N -> unconnected-(U2-PadL20)
- U2 pad N18: /FPGA/QDR SRAM/QDR_SYSCLK_P -> /FPGA/QDR SRAM/QDR_CQ_N
- U2 pad N19: /FPGA/QDR SRAM/QDR_SYSCLK_N -> unconnected-(U2-PadN19)
